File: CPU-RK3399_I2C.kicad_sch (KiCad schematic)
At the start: 18 parts, among them U1 RK3399

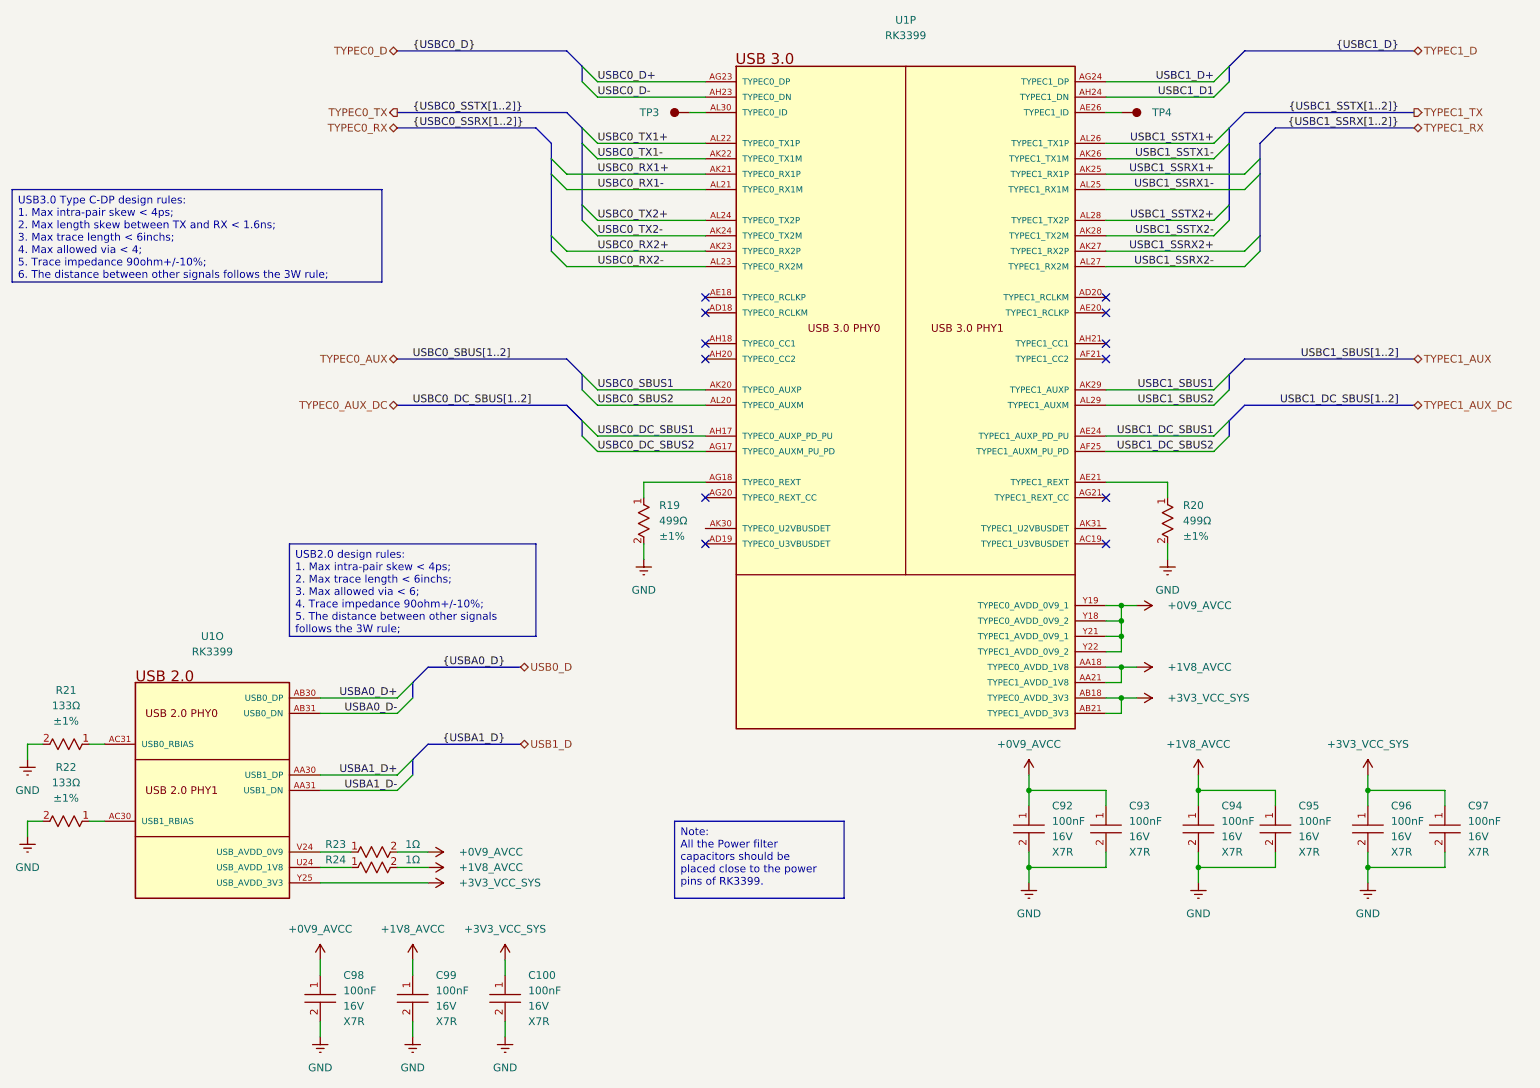
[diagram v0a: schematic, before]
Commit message: update schematic
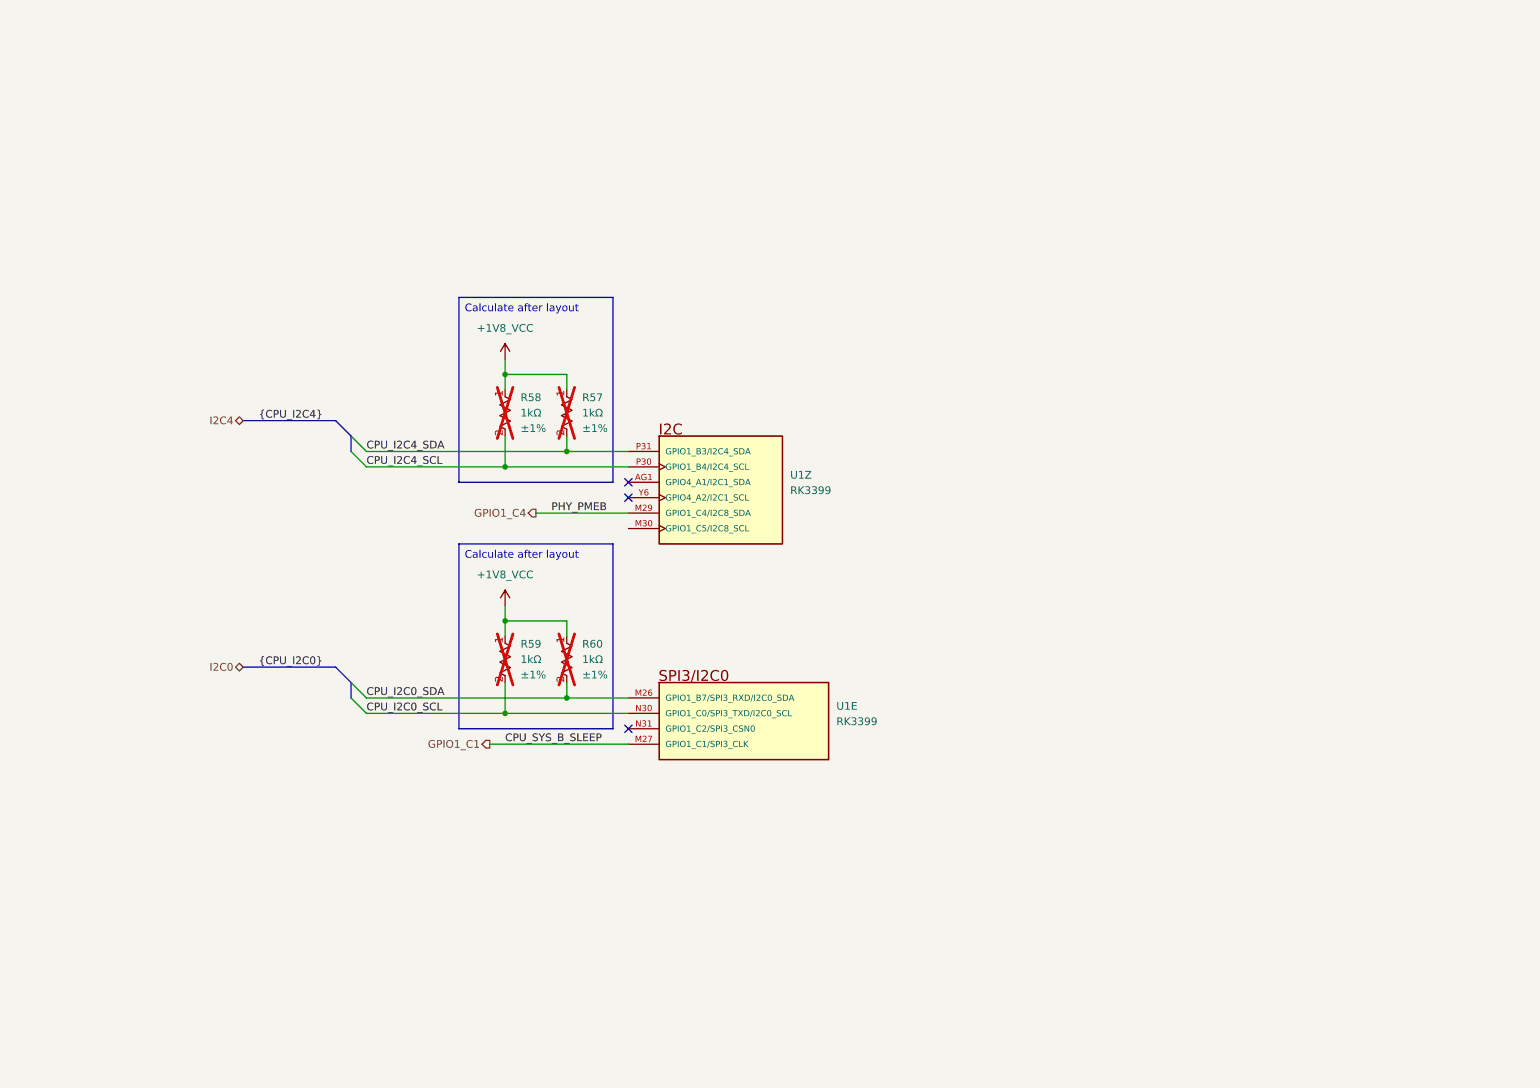
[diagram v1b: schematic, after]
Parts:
- removed C100, C92, C93, C94, C95, C96, C97, C98, C99: ~, footprints:CAPC1005X50N, symbol component_library:Capacitors/CL05B104KO5NNNC
- removed R19, R20: ~, footprints:RESC1005X35N, symbol component_library:Resistors/0402WGF4990TCE
- removed R21, R22: ~, footprints:RESC1005X35N, symbol component_library:Resistors/0402WGF1330TCE
- removed R23, R24: ~, footprints:, symbol component_library:Resistors/0603WAF100KT5E
- removed TP3, TP4: ~, footprints:, symbol component_library:Mechanical/Test_Point
- removed U1: RK3399, footprints:BGA828C65P31X31_2100X2100X161, symbol component_library:System On Chip (SoC)/RK3399
- added R57, R58, R59, R60: ~, footprints:RESC1005X35N, symbol component_library:Resistors/0402WGF1001TCE
- added U1: RK3399, footprints:BGA828C65P31X31_2100X2100X161, symbol component_library:System On Chip (SoC)/RK3399
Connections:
- new net +1V8_VCC: R57.1, R58.1, R59.1, R60.1
- new net CPU_I2C0_SCL: R59.2, U1.N30 (GPIO1_C0/SPI3_TXD/I2C0_SCL)
- new net CPU_I2C0_SDA: R60.2, U1.M26 (GPIO1_B7/SPI3_RXD/I2C0_SDA)
- new net CPU_I2C4_SCL: R58.2, U1.P30 (GPIO1_B4/I2C4_SCL)
- new net CPU_I2C4_SDA: R57.2, U1.P31 (GPIO1_B3/I2C4_SDA)
- new net GPIO1_C1: U1.M27 (GPIO1_C1/SPI3_CLK)
- new net GPIO1_C4: U1.M29 (GPIO1_C4/I2C8_SDA)
- no-connect marks 12 -> 3
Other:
- title: CPU-RK3399 USB Controller -> CPU-RK3399 I2C Controller

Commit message: design PMIC
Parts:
- added Q1: ~, footprints:, symbol component_library:FETs/WNM2021-3/TR
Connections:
- net +1V8_VCC: now also Q1.G (Gate)
- net GPIO1_C4: now also Q1.D (Drain); no longer U1.M29 (GPIO1_C4/I2C8_SDA)
- net GPIO1_C5: now reaches U1.M30 (GPIO1_C5/I2C8_SCL)
- new net: Q1.S (Source), U1.M29 (GPIO1_C4/I2C8_SDA)
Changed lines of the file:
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@@
+	(wire
+		(pts
+			(xy 119.38 99.06) (xy 134.62 99.06)
+		)
+		(stroke
+			(width 0)
+			(type default)
+		)
+	)
 	(wire
 		(pts
@@
 	(wire
 		(pts
-			(xy 119.38 96.52) (xy 134.62 96.52)
-		)
-		(stroke
-			(width 0)
-			(type default)
-		)
-	)
-	(wire
-		(pts
 			(xy 114.3 88.9) (xy 134.62 88.9)
 		)
@@
 	(wire
 		(pts
+			(xy 81.28 88.9) (xy 81.28 91.44)
+		)
+		(stroke
+			(width 0)
+			(type default)
+		)
+	)
+	(wire
+		(pts
 			(xy 114.3 73.66) (xy 114.3 76.2)
 		)
@@
 		)
 	)
+	(wire
+		(pts
+			(xy 60.96 96.52) (xy 76.2 96.52)
+		)
+		(stroke
+			(width 0)
+			(type default)
+		)
+	)
 	(bus
 		(pts
@@
 	(wire
 		(pts
+			(xy 83.82 96.52) (xy 134.62 96.52)
+		)
+		(stroke
+			(width 0)
+			(type default)
+		)
+	)
+	(wire
+		(pts
 			(xy 124.46 83.82) (xy 124.46 86.36)
 		)
@@
 			(width 0)
 			(type default)
+		)
+	)
+	(label "PHY_PMEB"
+		(at 63.5 96.52 0)
+		(effects
+			(font
+				(size 1.27 1.27)
+			)
+			(justify left bottom)
 		)
 	)
@@
 		)
 	)
-	(label "PHY_PMEB"
-		(at 121.92 96.52 0)
+	(label "PMIC_INT#"
+		(at 121.92 99.06 0)
 		(effects
 			(font
@@
 		)
 	)
+	(hierarchical_label "GPIO1_C5"
+		(shape input)
+		(at 119.38 99.06 180)
+		(effects
+			(font
+				(size 1.27 1.27)
+			)
+			(justify right)
+		)
+	)
 	(hierarchical_label "GPIO1_C4"
 		(shape output)
-		(at 119.38 96.52 180)
+		(at 60.96 96.52 180)
 		(effects
 			(font
@@
 	)
 	(symbol
+		(lib_id "component_library:FETs/WNM2021-3/TR")
+		(at 78.74 91.44 90)
+		(mirror x)
+		(unit 1)
+		(exclude_from_sim no)
+		(in_bom yes)
+		(on_board yes)
+		(dnp no)
+		(property "Reference" "Q1"
+			(at 80.0099 97.79 0)
+			(effects
+				(font
+					(size 1.27 1.27)
+				)
+				(justify left)
+			)
+		)
+		(property "Value" "~"
+			(at 78.74 91.44 0)
+			(effects
+				(font
+					(size 1.27 1.27)
+				)
+				(hide yes)
+			)
+		)
+		(property "Footprint" "footprints:"
+			(at 78.74 91.44 0)
+			(effects
+				(font
+					(size 1.27 1.27)
+				)
+				(hide yes)
+			)
+		)
+		(property "Datasheet" ""
+			(at 78.74 91.44 0)
+			(effects
+				(font
+					(size 1.27 1.27)
+				)
+				(hide yes)
+			)
+		)
+		(property "Description" "-55℃~+150℃ 1 N-channel 1.15nC@4.5V 20V 320mΩ@1.8V 370mW 50pF 850mV 890mA 8pF N-Channel SOT-323 MOSFETs ROHS"
+			(at 78.74 91.44 0)
+			(effects
+				(font
+					(size 1.27 1.27)
+				)
+				(hide yes)
+			)
+		)
+		(pin "D"
+		)
+		(pin "G"
+		)
+		(pin "S"
+		)
+		(instances
+			(project ""
+				(path "/ebc9dc57-8b05-484a-a5cd-c53b1efc71d3/a7299b18-4123-434b-8c69-0b9524fffa12/34360fb0-b2c5-4c89-ba9d-b3004bec58f5"
+					(reference "Q1")
+					(unit 1)
+				)
+			)
+		)
+	)
+	(symbol
 		(lib_id "component_library:Resistors/0402WGF1001TCE")
 		(at 124.46 116.84 270)
@@
 					(unit 1)
 				)
+			)
+		)
+	)
+	(symbol
+		(lib_id "power:+1V0")
+		(at 81.28 88.9 0)
+		(unit 1)
+		(exclude_from_sim no)
+		(in_bom yes)
+		(on_board yes)
+		(dnp no)
+		(property "Reference" "#PWR0131"
+			(at 81.28 92.71 0)
+			(effects
+				(font
+					(size 1.27 1.27)
+				)
+				(hide yes)
+			)
+		)
+		(property "Value" "+1V8_VCC"
+			(at 81.28 83.82 0)
+			(effects
+				(font
+					(size 1.27 1.27)
+				)
+			)
+		)
+		(property "Footprint" ""
+			(at 81.28 88.9 0)
+			(effects
+				(font
+					(size 1.27 1.27)
+				)
+				(hide yes)
+			)
+		)
+		(property "Datasheet" ""
+			(at 81.28 88.9 0)
+			(effects
+				(font
+					(size 1.27 1.27)
+				)
+				(hide yes)
+			)
+		)
+		(property "Description" "Power symbol creates a global label with name \"+1V0\""
+			(at 81.28 88.9 0)
+			(effects
+				(font
+					(size 1.27 1.27)
+				)
+				(hide yes)
+			)
+		)
+		(pin "1"
+		)
+		(instances
+			(project "VESA-SBC3399"
+				(path "/ebc9dc57-8b05-484a-a5cd-c53b1efc71d3/a7299b18-4123-434b-8c69-0b9524fffa12/34360fb0-b2c5-4c89-ba9d-b3004bec58f5"
+					(reference "#PWR0131")
+					(unit 1)
+				)
